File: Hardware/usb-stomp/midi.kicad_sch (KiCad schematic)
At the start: 16 parts, among them J5 AudioJack4, J6 AudioJack4, U201 74AHCT2G125, U4 TLP2310

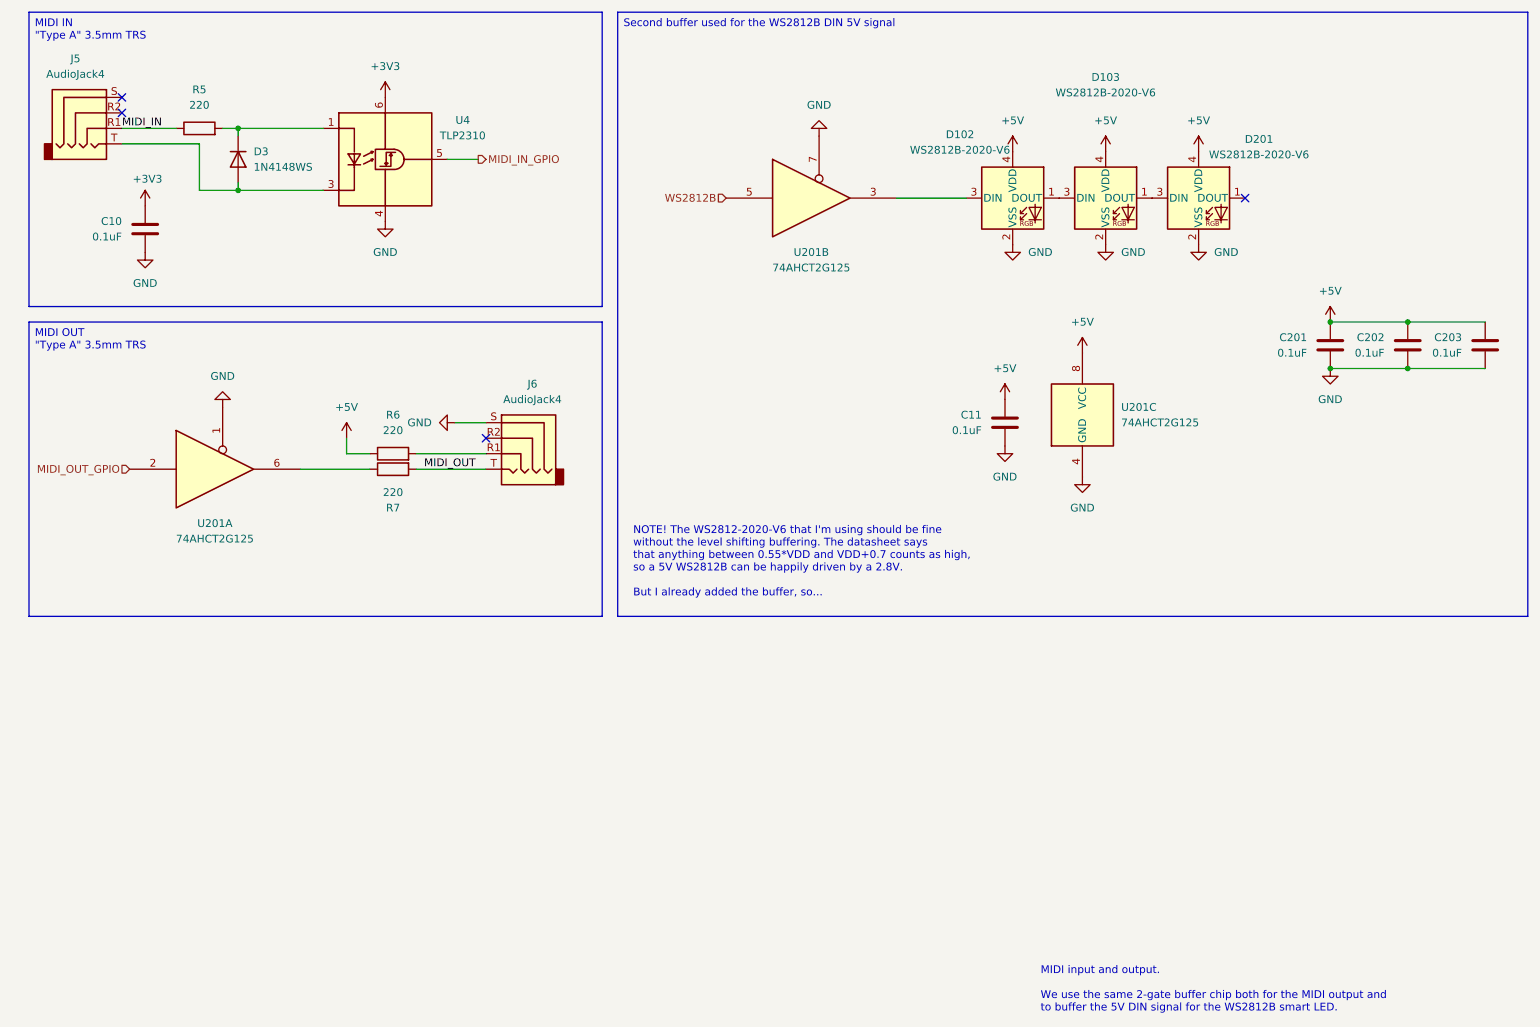
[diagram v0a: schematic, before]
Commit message: Let's re-do the usb-stomp board without the flex board
It was a teaching experience, but I guess the lesson was "don't do
that".  Let's just turn it into a straightforward simple single board.

I did decide to try a buck regulator, and I'm also playing with adding
support for a remote stomp switch or expression pedal.  I'm trying to do
it in a way that pretty much anything could be made to work - a single
remote stomp over a TS 1/4" cable, or a dual remote stomp over a TRS
one.  Or an expression pedal. But maybe I screwed that thing up.

The TRS Typa-A midi ports remain for remote control, but I'm thinking
that it shouldn't be too hard to teach WebMIDI to set up a model where
the remote stomp / expression pedal can control some arbitrary pot
value in the scene.

There's also a rotary encoder for the same reason - program the scene to
make it be the master volume, or the noise gate level, or whatever.

Of course, that "program the scene" part is all just a nebulous plan.  I
don't actually support that yet.  SMOP.

Signed-off-by: Linus Torvalds <torvalds@linux-foundation.org>
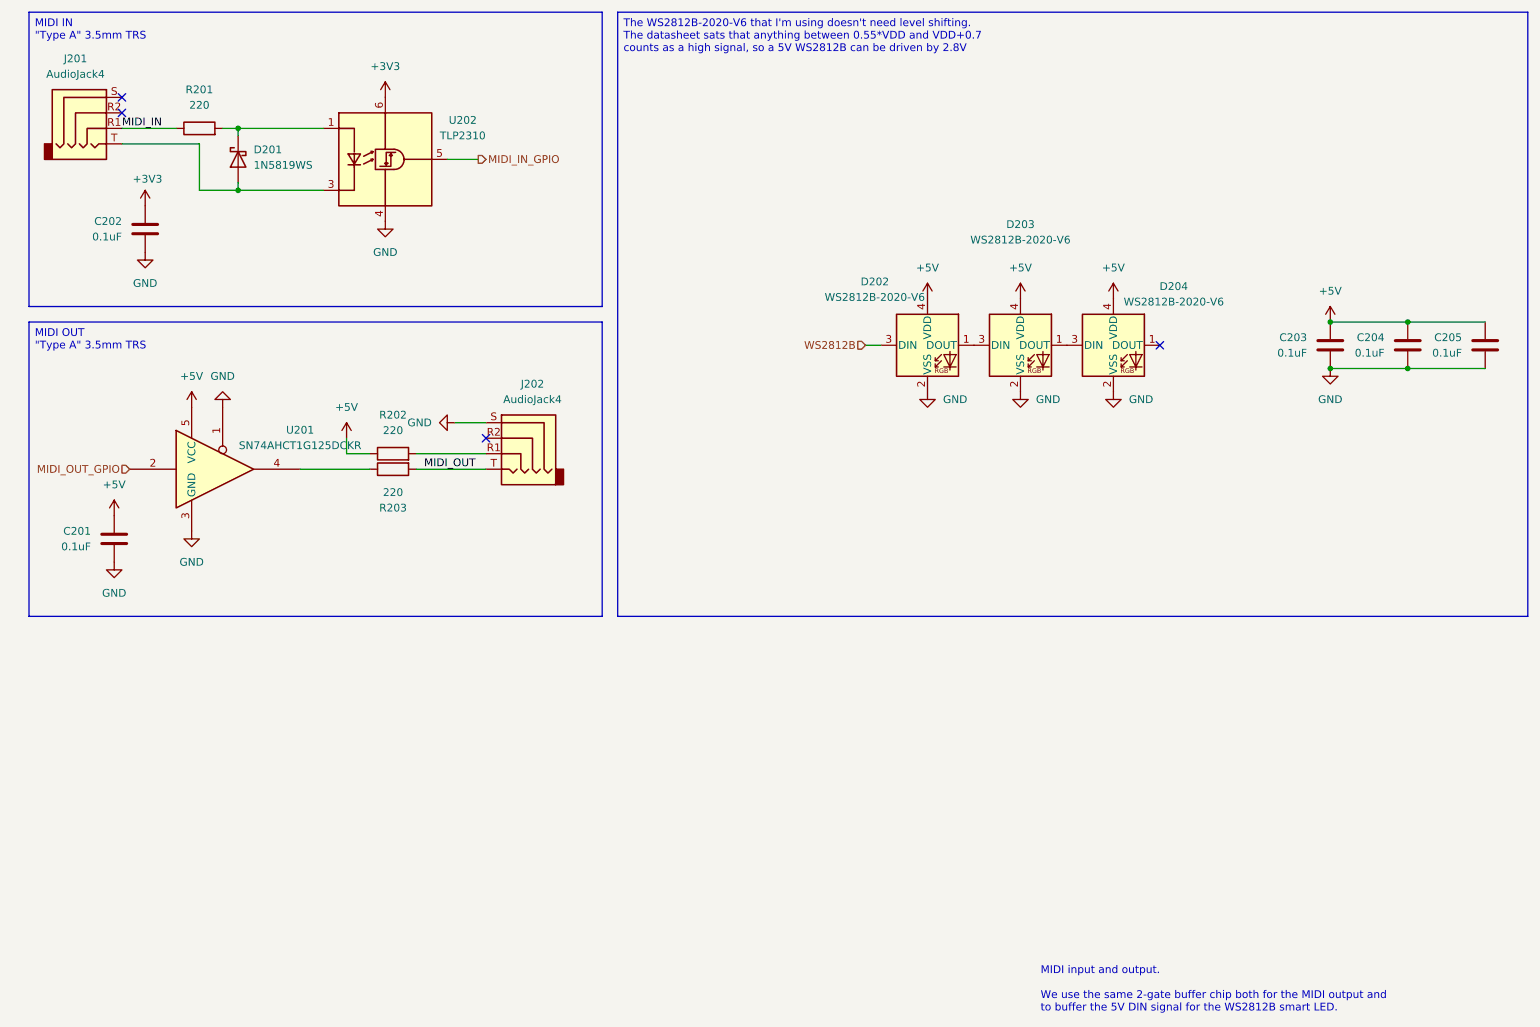
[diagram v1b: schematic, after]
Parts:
- removed D3: 1N4148WS, Diode_SMD:D_SOD-323, symbol Device:D
- removed U201: 74AHCT2G125, Package_SO:VSSOP-8_2.3x2mm_P0.5mm, symbol 74xGxx:74AUC2G125
- added D201: 1N5819WS, Diode_SMD:D_SOD-323, symbol Device:D_Schottky
- added U201: SN74AHCT1G125DCKR, Package_TO_SOT_SMD:SOT-353_SC-70-5, symbol 74xGxx:74AHCT1G125
- renumbered C11 to C201, C10 to C202, C201 to C203, C202 to C204, C203 to C205, D102 to D202, D103 to D203, D201 to D204, J5 to J201, J6 to J202, R5 to R201, R6 to R202, R7 to R203, U4 to U202
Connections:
- net +5V: now also U201.5 (VCC)
- net GND: now also U201.1, U201.3 (GND)
- net MIDI_OUT_GPIO: now also U201.2
- net WS2812B: now also D202.3 (DIN)
- net at R201.2, U202.1 (A): now also D201.1 (K)
- net at J201.T, U202.3 (K): now also D201.2 (A)
- net at R203.1: now also U201.4
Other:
- note removed: "NOTE! The WS2812-2020-V6 that I'm using should be fine without the level shifting buffering. The datasheet says that anything between 0.55*VDD and VDD+0.7 counts as high, so a 5V WS2812B can be happily driven by a 2.8V. But I already added the buffer, so..."
- moved on the sheet: C201, D202, D203, D204

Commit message: Fill in the manufacturer part numbers from the parts list
Every symbol that carries an LCSC PN now carries the manufacturer's own
part number beside it: 349 of them, against 17 before.  100 went into a
MANUFACTURER_PART_NUMBER field that already existed and was empty, and
232 needed the field creating, hidden, next to the LCSC PN it came
from.  Fifteen already agreed and were left alone.

The values come from Hardware/parts.txt, keyed on LCSC PN, taking the
part number as the last whitespace-separated token of each entry's
manufacturer line - which is what that line's shape means.

Two capacitors said "Samsung CL32B226KAJNNNE", with the maker's name
inside the part-number field; they now say CL32B226KAJNNNE like
everything else.  The manufacturer is not duplicated into the
schematics at all - parts.txt holds it, and the part number identifies
the part on its own.

Four one-off field names go with this, their contents now recorded
properly:

  Manufacturer / Part#  on the rotary board's L101, which is the Murata
                        LQM2MPN1R0MGHL
  Manufacutrer          the typo, on two inductors: DFE201612E-2R2M=P2
  Part                  on five Schottkys, saying "LRC LMBR130T1G"

That last one is worth a second look rather than a straight delete.
JLCPCB ships C191023 as a Guangdong Hottech 1N5819WS, so the schematic
was naming a different manufacturer's equivalent from the one actually
fitted.  The part number recorded here is what gets assembled; the
disagreement is written down in parts.txt next to the entry.

Netlists exported for all seven projects before and after: every net
and every pin on every net unchanged.

Signed-off-by: Linus Torvalds <torvalds@linux-foundation.org>
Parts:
- C201, C202, C203, C204, C205: MANUFACTURER_PART_NUMBER (none) -> GRM033Z71C104ME14D
- D201: MANUFACTURER_PART_NUMBER (none) -> 1N5819WS; Part LRC LMBR130T1G -> (none)
- D202, D203, D204: MANUFACTURER_PART_NUMBER (none) -> WS2812B-2020-V6
- J201, J202: MANUFACTURER_PART_NUMBER (none) -> PJ-320D
- R201, R202, R203: MANUFACTURER_PART_NUMBER (none) -> 0402WGF2200TCE
- U201: MANUFACTURER_PART_NUMBER (none) -> SN74AHCT1G125DCKR
- U202: MANUFACTURER_PART_NUMBER (none) -> TLP2310
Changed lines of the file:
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@@
+			)
+		)
+		(property "MANUFACTURER_PART_NUMBER" "SN74AHCT1G125DCKR"
+			(at 45.72 88.9 0)
+			(hide yes)
+			(show_name no)
+			(do_not_autoplace no)
+			(effects
+				(font
+					(size 1.27 1.27)
+				)
 			)
 		)
@@
 			)
 		)
-		(property "MANUFACTURER_PART_NUMBER" ""
+		(property "MANUFACTURER_PART_NUMBER" "GRM033Z71C104ME14D"
 			(at 27.94 100.33 0)
 			(hide yes)
@@
 			)
 		)
+		(property "MANUFACTURER_PART_NUMBER" "TLP2310"
+			(at 72.39 38.1 0)
+			(hide yes)
+			(show_name no)
+			(do_not_autoplace no)
+			(effects
+				(font
+					(size 1.27 1.27)
+				)
+			)
+		)
 		(pin "5"
 		)
@@
 			)
 		)
+		(property "MANUFACTURER_PART_NUMBER" "0402WGF2200TCE"
+			(at 73.66 86.36 90)
+			(hide yes)
+			(show_name no)
+			(do_not_autoplace no)
+			(effects
+				(font
+					(size 1.27 1.27)
+				)
+			)
+		)
 		(pin "1"
 		)
@@
 			)
 		)
-		(property "Part" "LRC LMBR130T1G"
+		(property "MANUFACTURER_PART_NUMBER" "1N5819WS"
 			(at 48.26 38.1 0)
 			(hide yes)
@@
 			)
 		)
-		(property "MANUFACTURER_PART_NUMBER" ""
+		(property "MANUFACTURER_PART_NUMBER" "GRM033Z71C104ME14D"
 			(at 33.02 49.53 0)
 			(hide yes)
@@
 			)
 		)
-		(property "MANUFACTURER_PART_NUMBER" ""
+		(property "MANUFACTURER_PART_NUMBER" "GRM033Z71C104ME14D"
 			(at 227.33 68.58 0)
 			(hide yes)
@@
 			)
 		)
-		(property "MANUFACTURER_PART_NUMBER" ""
+		(property "MANUFACTURER_PART_NUMBER" "GRM033Z71C104ME14D"
 			(at 240.03 68.58 0)
 			(hide yes)
@@
 			)
 		)
+		(property "MANUFACTURER_PART_NUMBER" "0402WGF2200TCE"
+			(at 41.91 33.02 90)
+			(hide yes)
+			(show_name no)
+			(do_not_autoplace no)
+			(effects
+				(font
+					(size 1.27 1.27)
+				)
+			)
+		)
 		(pin "1"
 		)
@@
 			)
 		)
+		(property "MANUFACTURER_PART_NUMBER" "0402WGF2200TCE"
+			(at 73.66 88.9 90)
+			(hide yes)
+			(show_name no)
+			(do_not_autoplace no)
+			(effects
+				(font
+					(size 1.27 1.27)
+				)
+			)
+		)
 		(pin "1"
 		)
@@
 		)
 		(property "LCSC PN" "C52917434"
+			(at 176.53 68.58 0)
+			(hide yes)
+			(show_name no)
+			(do_not_autoplace no)
+			(effects
+				(font
+					(size 1.27 1.27)
+				)
+			)
+		)
+		(property "MANUFACTURER_PART_NUMBER" "WS2812B-2020-V6"
 			(at 176.53 68.58 0)
 			(hide yes)
@@
 			)
 		)
+		(property "MANUFACTURER_PART_NUMBER" "PJ-320D"
+			(at 24.13 30.48 0)
+			(hide yes)
+			(show_name no)
+			(do_not_autoplace no)
+			(effects
+				(font
+					(size 1.27 1.27)
+				)
+			)
+		)
 		(pin "R2"
 		)
@@
 			)
 		)
+		(property "MANUFACTURER_PART_NUMBER" "PJ-320D"
+			(at 93.98 83.82 0)
+			(hide yes)
+			(show_name no)
+			(do_not_autoplace no)
+			(effects
+				(font
+					(size 1.27 1.27)
+				)
+			)
+		)
 		(pin "R2"
 		)
@@
 		)
 		(property "LCSC PN" "C52917434"
+			(at 191.77 68.58 0)
+			(hide yes)
+			(show_name no)
+			(do_not_autoplace no)
+			(effects
+				(font
+					(size 1.27 1.27)
+				)
+			)
+		)
+		(property "MANUFACTURER_PART_NUMBER" "WS2812B-2020-V6"
 			(at 191.77 68.58 0)
 			(hide yes)
@@
 			)
 		)
+		(property "MANUFACTURER_PART_NUMBER" "WS2812B-2020-V6"
+			(at 161.29 68.58 0)
+			(hide yes)
+			(show_name no)
+			(do_not_autoplace no)
+			(effects
+				(font
+					(size 1.27 1.27)
+				)
+			)
+		)
 		(pin "4"
 		)
@@
 			)
 		)
-		(property "MANUFACTURER_PART_NUMBER" ""
+		(property "MANUFACTURER_PART_NUMBER" "GRM033Z71C104ME14D"
 			(at 252.73 68.58 0)
 			(hide yes)
